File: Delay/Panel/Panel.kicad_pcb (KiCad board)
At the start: 2 copper layers, 192.7 x 128.5 mm, 0 parts

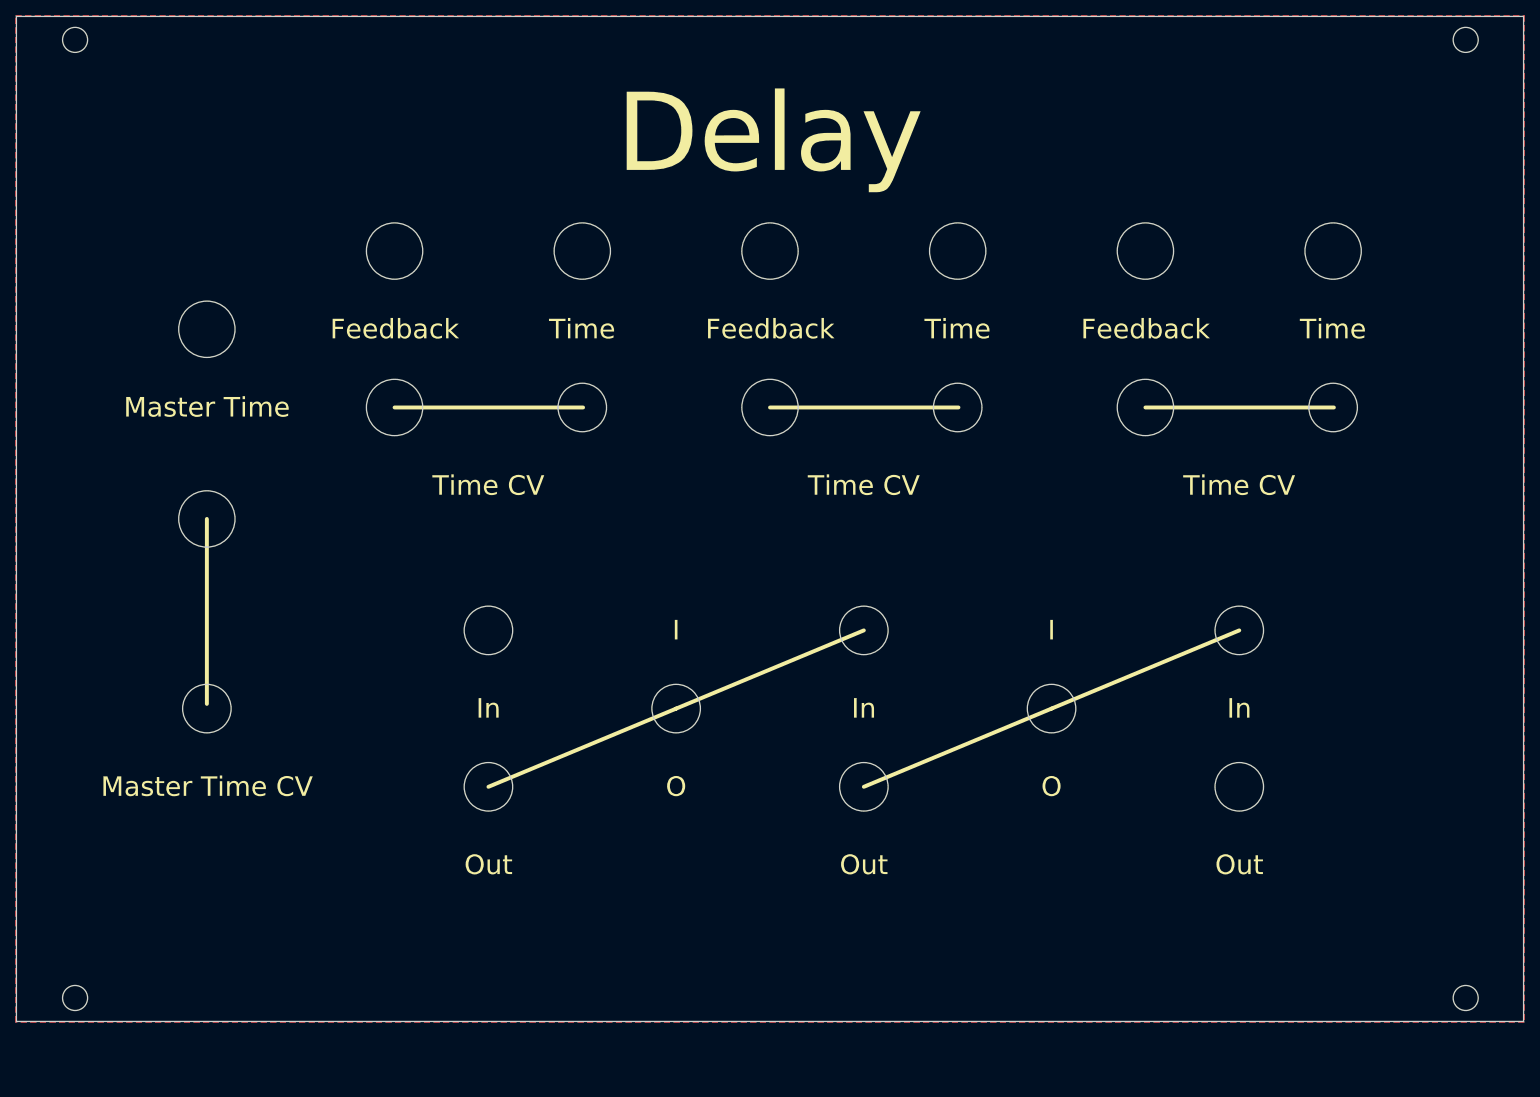
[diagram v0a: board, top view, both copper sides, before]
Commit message: Finish diode ladder filter
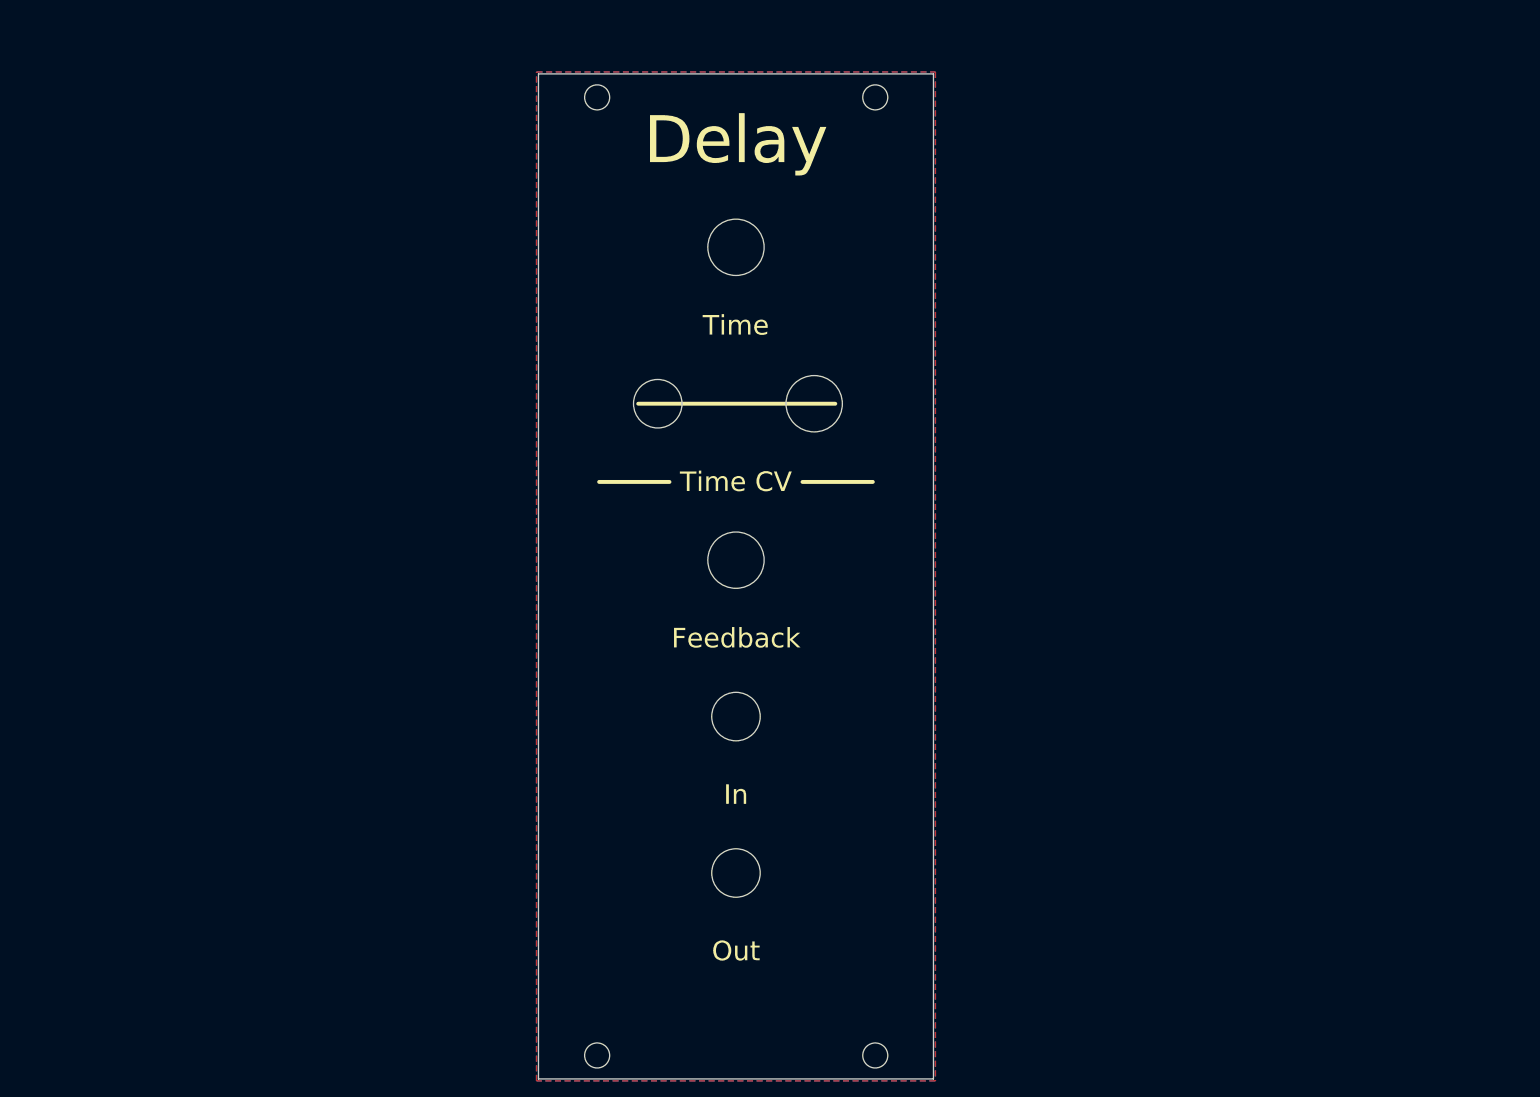
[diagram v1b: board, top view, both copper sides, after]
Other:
- board size 192.7 x 128.5 mm -> 50.5 x 128.5 mm
- board text removed: "I"
- board text removed: "Master Time"
- board text removed: "Master Time CV"
- board text removed: "O"
